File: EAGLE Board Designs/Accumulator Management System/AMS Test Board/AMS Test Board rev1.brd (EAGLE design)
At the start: 386.6 x 87.7 mm, 90 parts, among them J1 CONNECTOR-2__B2B-PH-K, J10 CONNECTOR-2__B2B-PH-K, J11 CONNECTOR-2__B2B-PH-K, J12 CONNECTOR-2__B2B-PH-K, J13 CONNECTOR-2__B2B-PH-K, J14 CONNECTOR-2__B2B-PH-K, J15 CONNECTOR-2__B2B-PH-K, J16 CONNECTOR-2__B2B-PH-K, J17 CONNECTOR-2__B2B-PH-K, J18 CONNECTOR-2__B2B-PH-K, J19 CONNECTOR-2__B2B-PH-K, J2 CONNECTOR-2__B2B-PH-K, J20 CONNECTOR-2__B2B-PH-K, J21 CONNECTOR-2__B2B-PH-K, J22 CONNECTOR-1_5222, J23 CONNECTOR-1_5222, J24 CONNECTOR-1_5222, J25 CONNECTOR-1_5222, J26 CONNECTOR-1_5222, J27 CONNECTOR-1_5222, J28 CONNECTOR-1_5222, J29 CONNECTOR-1_5222, J3 CONNECTOR-2__B2B-PH-K, J30 CONNECTOR-1_5222, J31 CONNECTOR-1_5222, J32 CONNECTOR-1_5222, J33 CONNECTOR-1_5222, J34 CONNECTOR-1_5222, J35 CONNECTOR-1_5222, J36 CONNECTOR-1_5222, J37 CONNECTOR-1_5222, J38 CONNECTOR-1_5222, J39 CONNECTOR-1_5222, J4 CONNECTOR-2__B2B-PH-K, J40 CONNECTOR-1_5222, J41 CONNECTOR-1_5222, J42 CONNECTOR-1_5222, J43 CONNECTOR-1_5222, J5 CONNECTOR-2__B2B-PH-K, J6 CONNECTOR-2__B2B-PH-K, J7 CONNECTOR-2__B2B-PH-K, J8 CONNECTOR-2__B2B-PH-K, J9 CONNECTOR-2__B2B-PH-K

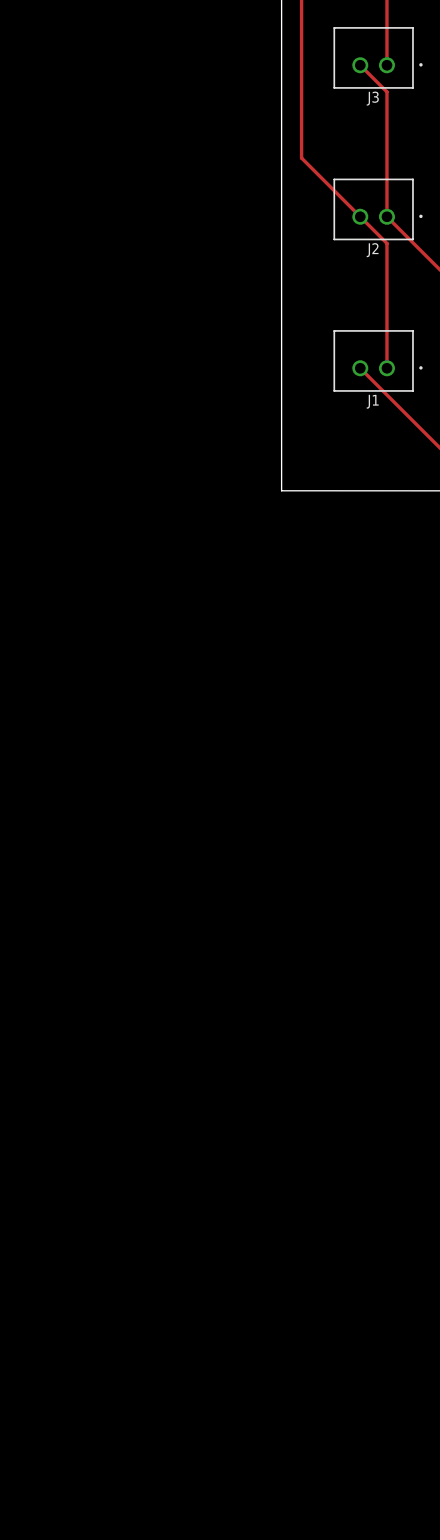
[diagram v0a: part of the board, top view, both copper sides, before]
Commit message: AMS Test Board Rev2 LTC6820 and Transformer Schematic
Recreated the schematic of the Teensy 4.0, LTC6820, and transformer from the Accumulator Control Unit.
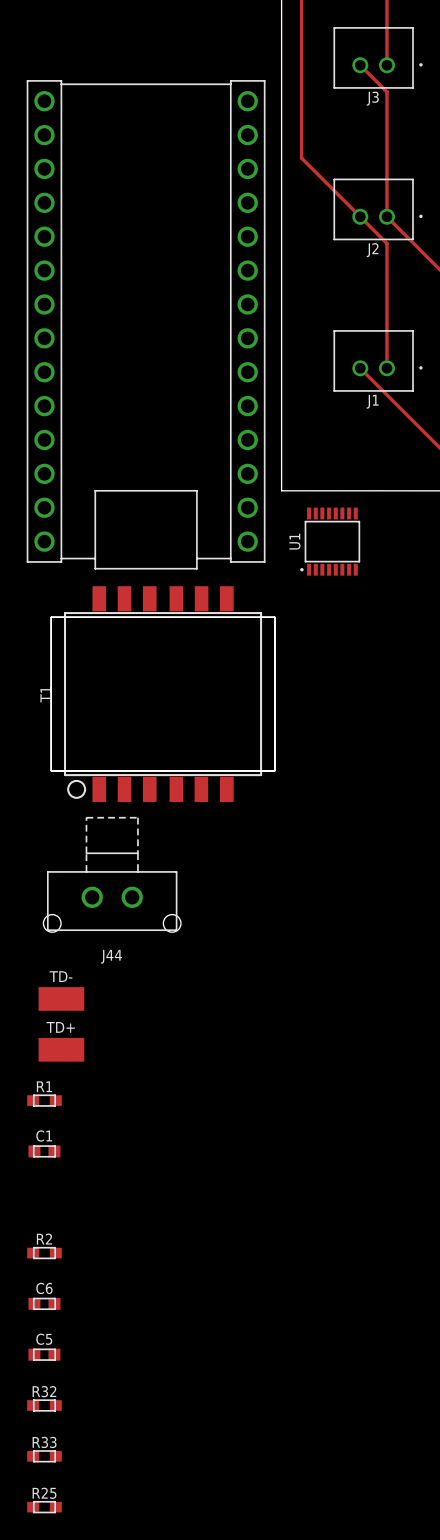
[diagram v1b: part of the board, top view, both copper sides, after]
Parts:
- added A1: TEENSY_4.0, HyTechDevices:TEENSY_SHORT
- added C1: CAPACITOR_0603_10V_10NF, HyTechDevices - Copy:0603-CAP
- added C5: CAPACITOR_0603_10V_0.1UF, HyTechDevices:0603-CAP
- added C6: CAPACITOR_0603_10V_10NF, HyTechDevices:0603-CAP
- added J44: CONNECTOR-2_MF_T_V_, HyTechDevices - Copy:MOLEX_MICROFIT_PTH_VERTICAL_02_SINGLE
- added R1: RESISTOR_0603_120, HyTechDevices:0603-RES
- added R2, R25: RESISTOR_0603_1K, HyTechDevices - Copy:0603-RES
- added R32, R33: RESISTOR_0603_2K, HyTechDevices:0603-RES
- added T1: TRANSFORMER_HM2112ZNLT_AIRGAP, HyTechDevices:HM2112ZNLT_AIRGAP
- added TD+, TD-: TEST_POINT, HyTechDevices - Copy:MICRO_MINIATURE
- added U1: LTC6820, HyTechDevices:MSOP-16
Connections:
- new net +3V3: A1.3.3V, C5.1, C6.2, R32.2, R33.2, U1.1, U1.12, U1.6, U1.7, U1.8, U1.9
- new net +5V: A1.VIN
- new net GND: A1.AGND/GND, A1.GND, C1.2, C5.2, C6.1, R2.2
- new net N$23: C1.1, T1.11
- new net N$24: A1.D13, U1.4
- new net N$25: A1.D12, R32.1, U1.3
- new net N$26: A1.D11, R33.1, U1.2
- new net N$27: A1.D10, U1.5
- new net N$28: U1.13, U1.14
- new net N$29: J44.2, R1.1, T1.3
- new net N$30: R25.1, U1.16
- new net N$31: R2.1, R25.2, U1.15
- new net N$34: J44.1, R1.2, T1.1
- new net N$35: T1.12, U1.11
- new net N$36: T1.10, U1.10
- new net TD+: TD+.1
- new net TD-: TD-.1

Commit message: AMS Test Board Rev2
Placed components onto the board in a general layout and started routing.
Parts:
- moved TD+ 427.1 mm to (407.7, 7.62)
- moved TD- 427.1 mm to (407.7, 11.4)
- moved A1 401.2 mm to (381.3, 38.1), turned to 180 degrees
- moved C6 390.6 mm to (359.4, 40.6)
- moved R25 385.6 mm to (359.0, 5.59), turned to 180 degrees
- moved R32 385.0 mm to (359.0, 10.3), turned to 180 degrees
- moved C5 384.4 mm to (349.2, 49.5)
- moved R33 382.4 mm to (355.6, 10.2), turned to 180 degrees
- moved R2 378.0 mm to (355.0, 5.59), turned to 180 degrees
- moved C1 375.0 mm to (350.6, 20.4), turned to 180 degrees
- moved R1 364.2 mm to (342.9, 5.08)
- moved J44 358.1 mm to (342.9, 11.4)
- moved T1 354.0 mm to (342.1, 30.5), turned to 270 degrees
- moved U1 353.4 mm to (356.1, 24.3), turned to 90 degrees
- moved U$6 49.6 mm to (415.8, 39.4), flipped to the bottom
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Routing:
- net +3V3: track 0.00 -> 88.1 mm
- net N$34: track 0.00 -> 55.2 mm
- net N$26: track 0.00 -> 45.1 mm
- net N$24: track 0.00 -> 38.3 mm
- net N$29: track 0.00 -> 31.0 mm
- net N$25: track 0.00 -> 24.0 mm
- net N$27: track 0.00 -> 20.3 mm
- net GND: track 0.00 -> 16.3 mm

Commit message: Update AMS Test Board rev1.brd
Did some more component routing
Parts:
- moved C5 14.8 mm to (356.1, 36.4), turned to 180 degrees
- moved C1 10.2 mm to (356.1, 29.1)
- moved R32 9.60 mm to (356.1, 19.4)
- moved C6 8.54 mm to (356.1, 32.8)
- moved R25 7.45 mm to (356.1, 12.4), turned to 0 degrees
- moved R33 5.99 mm to (356.1, 16.1)
- moved R2 3.37 mm to (356.1, 8.76)
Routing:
- net N$25: track 24.0 -> 48.9 mm
- net GND: track 16.3 -> 40.5 mm
- net N$31: track 0.00 -> 22.8 mm
- net N$30: track 0.00 -> 12.2 mm
- net +3V3: track 88.1 -> 81.8 mm
- net N$26: track 45.1 -> 50.6 mm

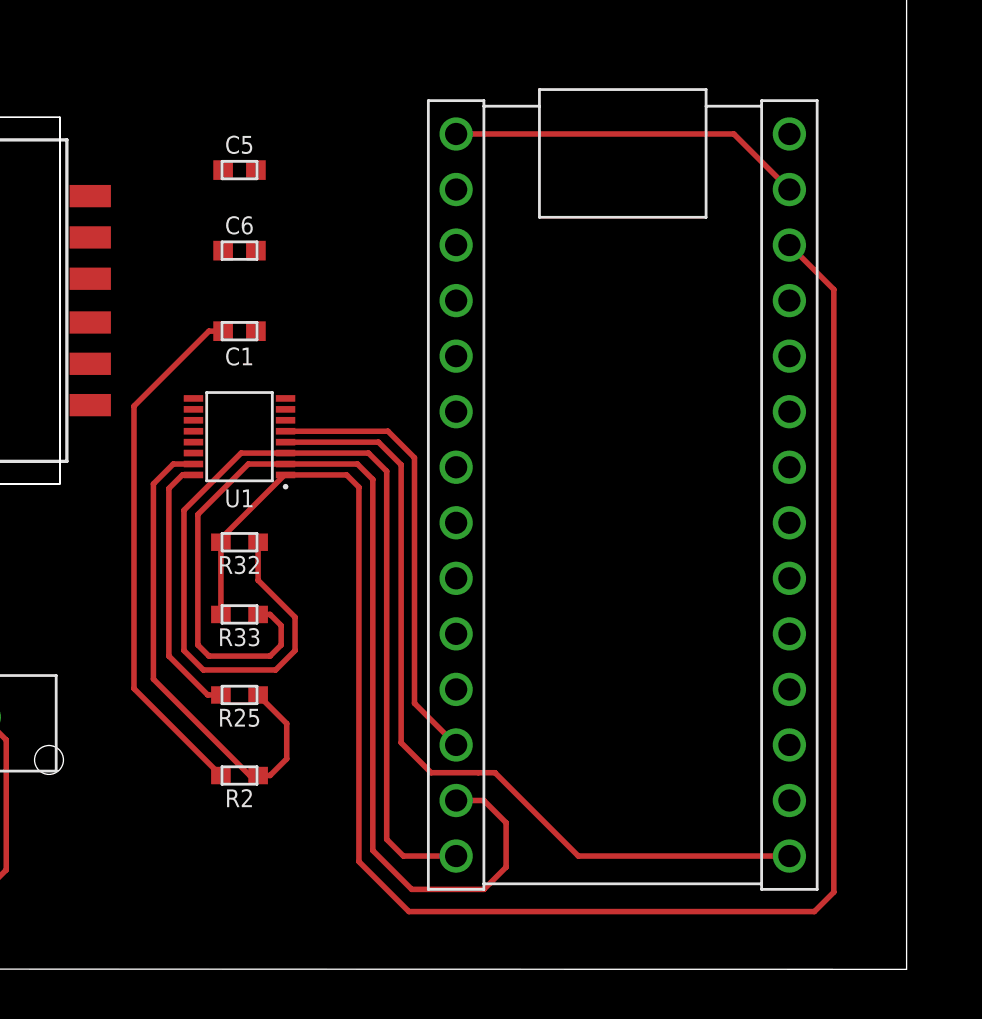
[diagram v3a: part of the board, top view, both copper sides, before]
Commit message: Update AMS Test Board rev1.brd
Drafted a possible routing design for the right ACU sector of the board.
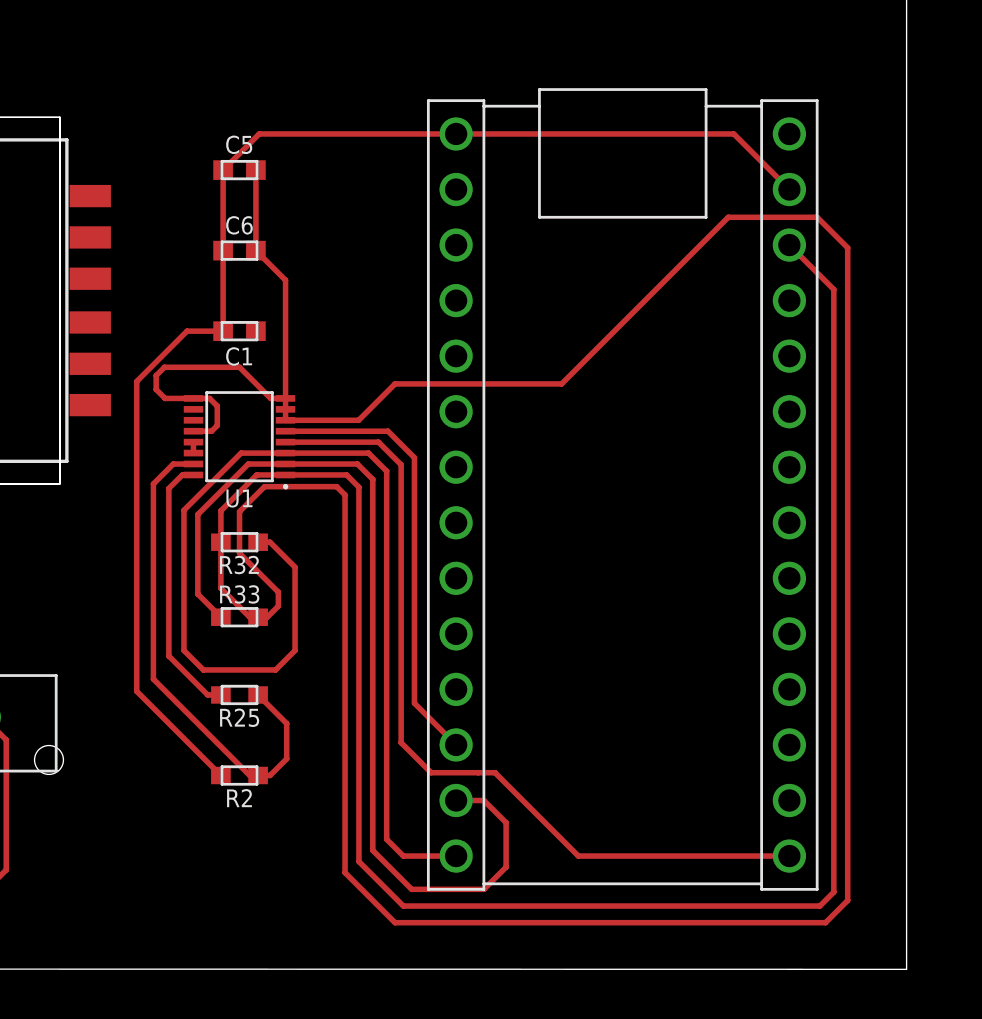
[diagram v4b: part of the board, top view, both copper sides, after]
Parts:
- moved R33 0.13 mm to (356.1, 16.0), turned to 0 degrees
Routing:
- net +3V3: track 81.8 -> 221.1 mm
- net GND: track 40.5 -> 59.7 mm
- net N$26: track 50.6 -> 43.3 mm
- net N$28: track 0.00 -> 0.50 mm

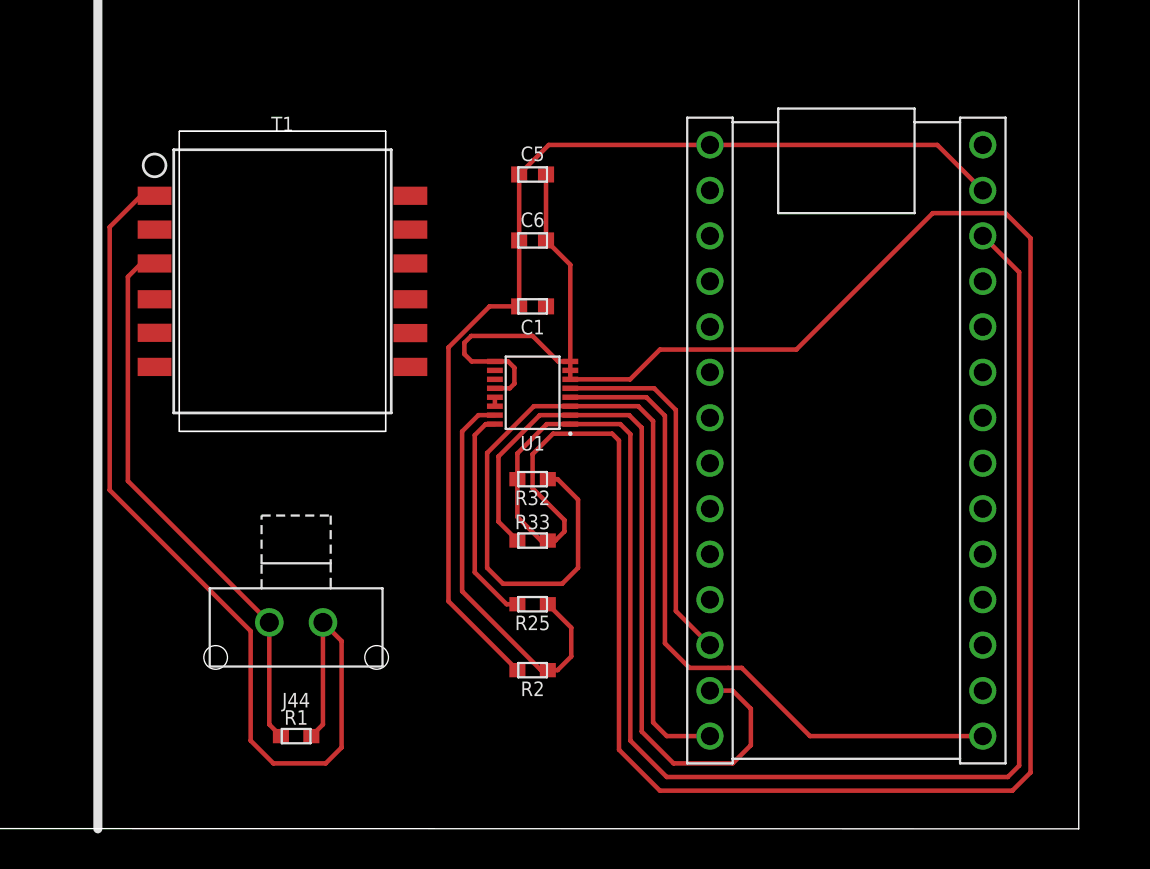
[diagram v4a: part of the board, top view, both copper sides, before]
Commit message: AMS Test Board rev2
Undid the routing for rev2
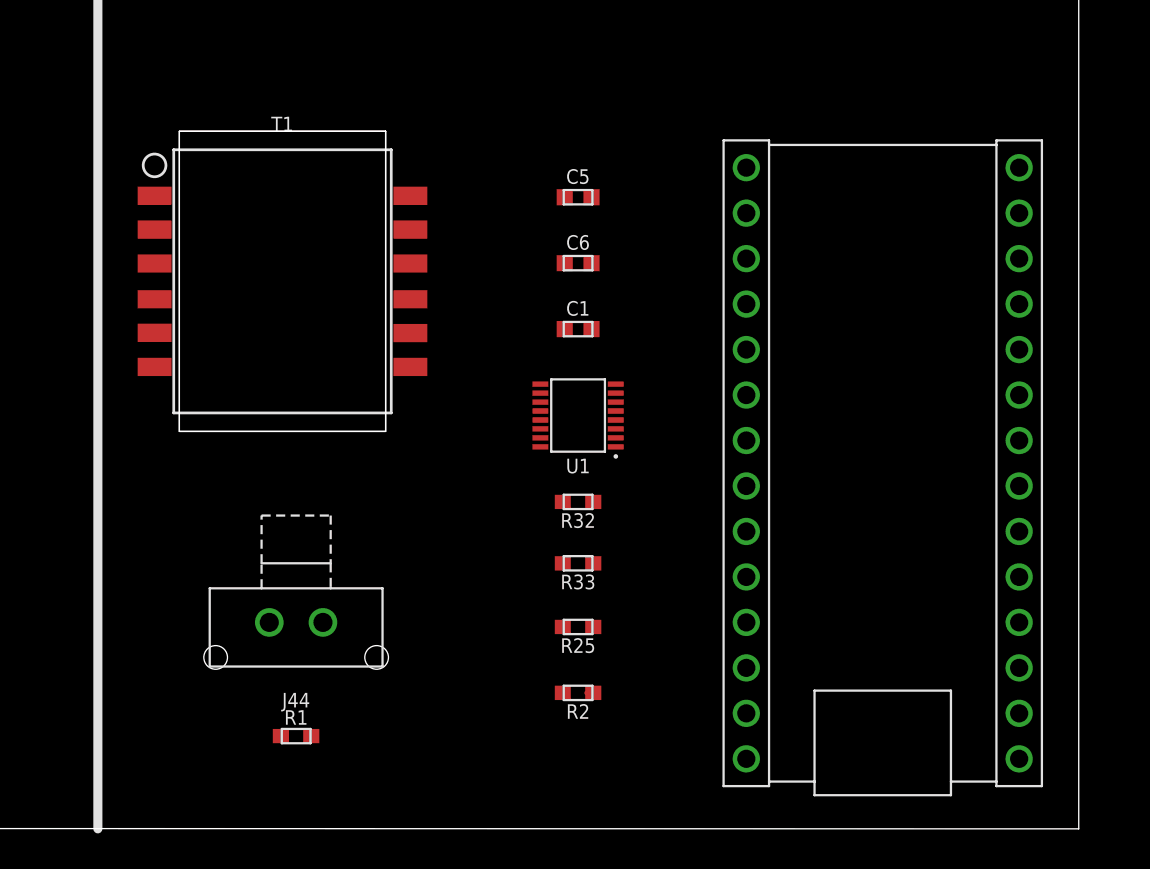
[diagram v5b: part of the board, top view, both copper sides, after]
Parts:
- moved A1 36.7 mm to (368.0, 3.81), turned to 0 degrees
- moved U1 2.84 mm to (358.6, 23.0)
- moved C1 2.84 mm to (358.6, 27.8), turned to 0 degrees
- moved C6 2.84 mm to (358.6, 31.5)
- moved R2 2.84 mm to (358.6, 7.49)
- moved R25 2.84 mm to (358.6, 11.2)
- moved R32 2.84 mm to (358.6, 18.2)
- moved R33 2.84 mm to (358.6, 14.7)
- moved C5 2.84 mm to (358.6, 35.2)
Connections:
- net +5V renamed VIN
- net N$35 renamed IP
- net N$36 renamed IM
- removed net N$29: J44.2, R1.1, T1.3
- removed net N$34: J44.1, R1.2, T1.1
- net TD+: now also J44.1, R1.2, T1.1
- net TD-: now also J44.2, R1.1, T1.3
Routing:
- net +3V3: track 221.1 -> 0.00 mm
- net GND: track 59.7 -> 0.00 mm
- net N$34: track 55.2 -> 0.00 mm
- net N$25: track 49.2 -> 0.00 mm
- net N$26: track 43.3 -> 0.00 mm
- net N$24: track 38.3 -> 0.00 mm
- net N$29: track 31.0 -> 0.00 mm
- net N$31: track 22.8 -> 0.38 mm
- net N$27: track 20.3 -> 0.00 mm
- net N$30: track 12.2 -> 0.00 mm
- net TD+: track 0.00 -> 1.02 mm
- net TD-: track 0.00 -> 0.75 mm
- net N$28: track 0.50 -> 0.00 mm

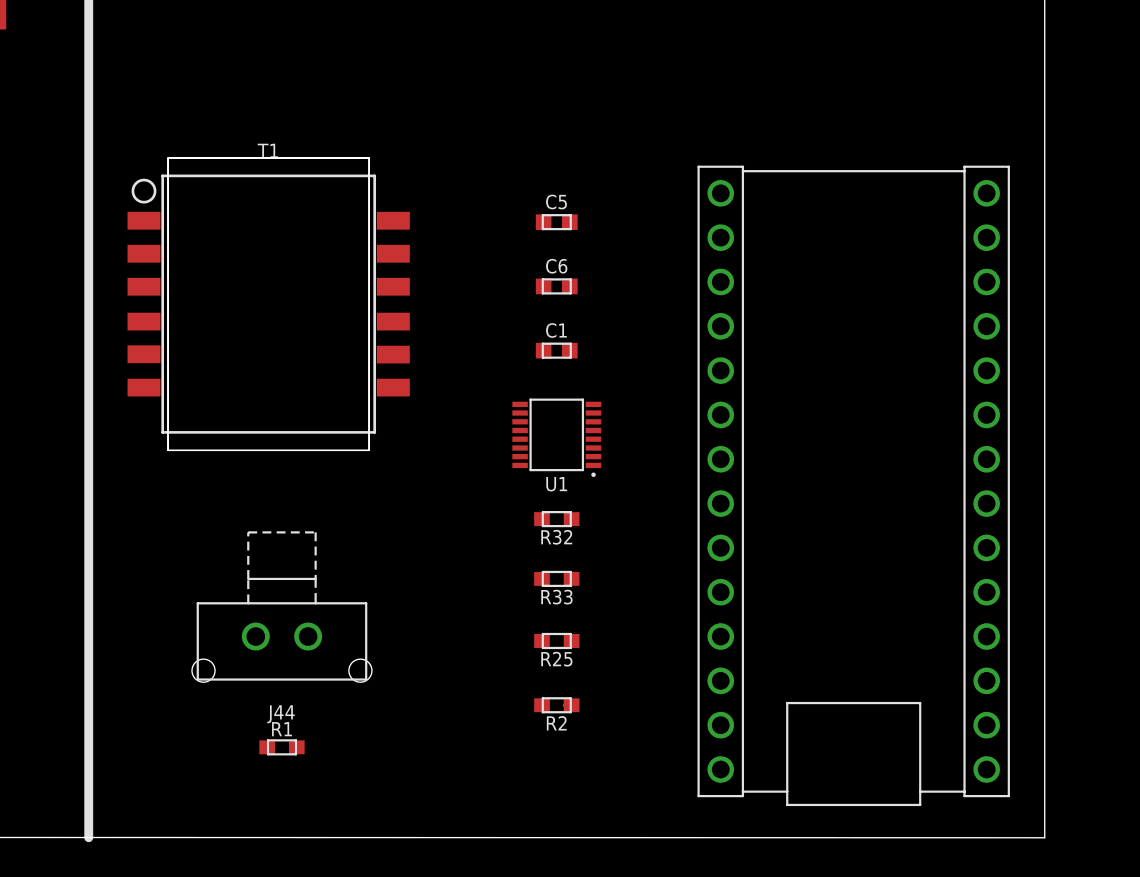
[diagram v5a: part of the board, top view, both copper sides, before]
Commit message: Update AMS Test Board rev1.brd
Created a GND polygon on the bottom layer to connect all the GND for easier routing on the top layer.
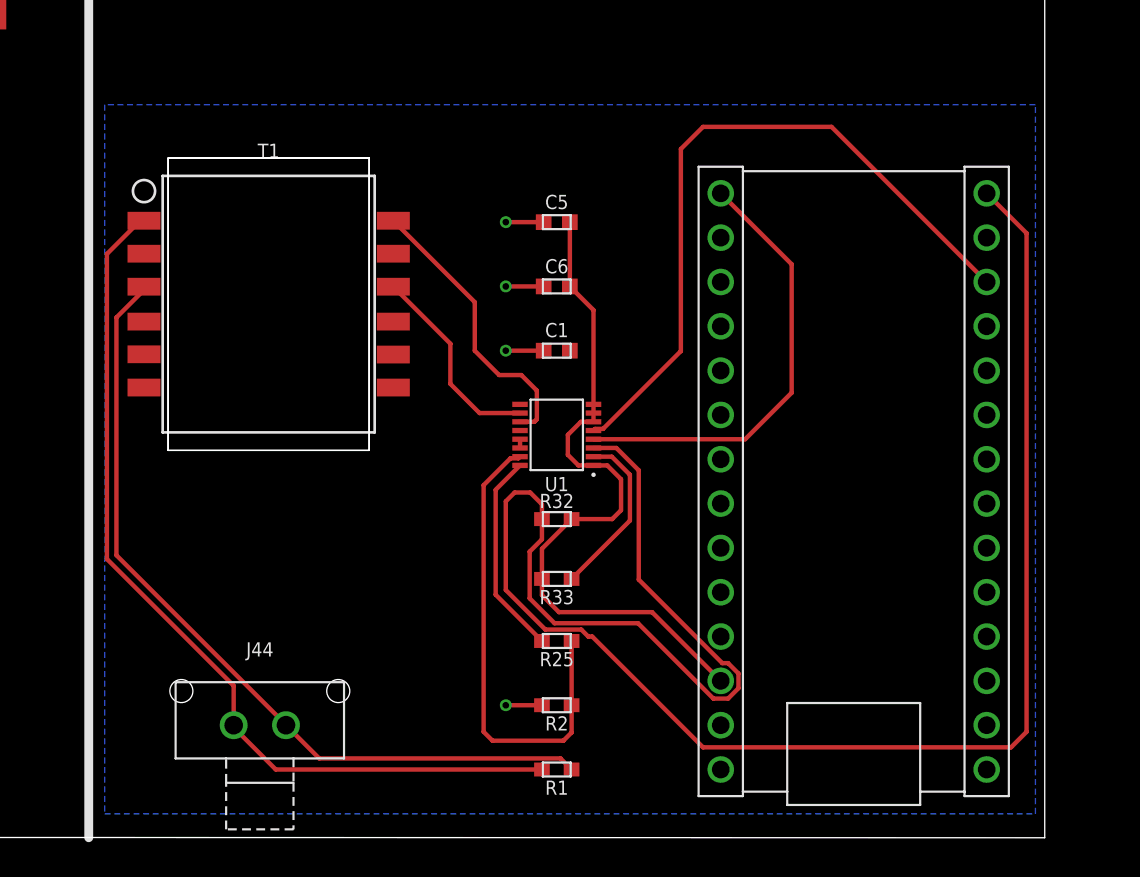
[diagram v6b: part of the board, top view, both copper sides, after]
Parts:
- moved R1 15.8 mm to (358.6, 3.81), turned to 180 degrees
- moved J44 5.24 mm to (341.6, 6.35), turned to 180 degrees
- turned C1 to 180 degrees
- turned R32 to 0 degrees
- turned R33 to 180 degrees
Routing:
- net N$25: track 0.00 -> 111.8 mm
- net TD+: track 1.02 -> 52.3 mm
- net TD-: track 0.75 -> 48.0 mm
- net +3V3: track 0.00 -> 40.7 mm
- net N$27: track 0.00 -> 40.2 mm
- net N$31: track 0.38 -> 27.6 mm
- net N$24: track 0.00 -> 25.6 mm
- net IP: track 0.00 -> 16.6 mm
- net N$30: track 0.00 -> 11.7 mm
- net IM: track 0.02 -> 11.6 mm
- net N$26: track 0.00 -> 9.87 mm
- net GND: track 0.00 -> 8.58 mm, vias 0 -> 4
- net N$28: track 0.00 -> 0.50 mm
- added copper zone on layer 16, net GND
